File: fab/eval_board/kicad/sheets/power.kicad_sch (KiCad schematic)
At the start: 9 parts, among them J1 Barrel_Jack_12V, U10 ADP7118_0.9V, U11 TPS7A2018_1.8V_NCE, U12 TPS7A2010_1.0V, U13 TPS7A3301_3.3V, U14 TPS7A2018_1.8V_FPGA, U15 TPS54360

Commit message: fix: regenerate KiCad files in valid KiCad 8 format
- Rewrote all .kicad_sch files with proper lib_symbols sections,
  symbol instances, wires, hierarchical sheet references, and
  power port definitions (removed invalid ';;' comment syntax)
- Fixed .kicad_pcb: removed comment lines, added 922 missing net
  definitions, fixed gr_text justify format
- Regenerated Gerbers from fixed PCB using kicad-cli (30 files)
- All files validated with kicad-cli: schematic exports 5-page PDF,
  PCB exports SVG, DRC/ERC both run without parse errors
- Added regenerate_kicad.py generator script for reproducibility

Co-Authored-By: Bola Olatunji <bola.olatunji@ai.lightos.sh>
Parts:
- removed U11: TPS7A2018_1.8V_NCE, Package_TO_SOT_SMD:SOT-23-5, symbol Regulator_Linear:TPS7A20xx
- removed U12: TPS7A2010_1.0V, Package_TO_SOT_SMD:SOT-23-5, symbol Regulator_Linear:TPS7A20xx
- removed U14: TPS7A2018_1.8V_FPGA, Package_TO_SOT_SMD:SOT-23-5, symbol Regulator_Linear:TPS7A20xx
- added C1, C2, C3, C4, C5, C6: 100nF, Capacitor_SMD:C_0402_1005Metric, symbol Device:C
- added C20: 100uF, Capacitor_SMD:C_1206_3216Metric, symbol Device:C
- added D1: Green, LED_SMD:LED_0603_1608Metric, symbol Device:LED
- added R20: 1k, Resistor_SMD:R_0402_1005Metric, symbol Device:R
- added U11: TPS7A2018_3V3_1V8, Package_TO_SOT_SMD:SOT-23-5, symbol Regulator_Linear:TPS7A2018
- added U12: TPS7A2010_1V8_1V0, Package_TO_SOT_SMD:SOT-23-5, symbol Regulator_Linear:TPS7A2010
- added U14: TPS7A2018_3V3_1V8_FPGA, Package_TO_SOT_SMD:SOT-23-5, symbol Regulator_Linear:TPS7A2018
- L1: value 4.7uH -> 10uH; footprint Inductor_SMD:L_5x5mm -> Inductor_SMD:L_Wuerth_WE-LHMI_7050; MPN 744043004R7 -> 744373460100
- U10: value ADP7118_0.9V -> ADP7118_5V_0V9
- U13: value TPS7A3301_3.3V -> TPS7A3301_5V_3V3; footprint Package_TO_SOT_SMD:SOT-23-5 -> Package_TO_SOT_SMD:SOT-223-5; MPN TPS7A3301DBVR -> TPS7A3301DCQR
- U15: value TPS54360 -> TPS54360_12V_5V; MPN TPS54360DDAR -> TPS54360BDDAR
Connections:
- new net: F1.1, J1.1
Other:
- note removed: "POWER SEQUENCING: 12V → 5V (U15 buck, <1ms) 5V → 3.3V (U13 LDO, <0.5ms) 3.3V → 1.8V (U11/U14, <0.5ms) 1.8V → 1.0V (U12, <0.5ms) 5V → 0.9V (U10, <0.5ms) EN pins: tied to upstream rail for natural sequencing"
- note removed: "See BOM for complete capacitor placement. Decoupling: 100nF + 10uF per rail. Placement: Within 3mm of regulator output pin."
- title: Power Supply — LightRail Eval Board -> Power Supply - LightRail Eval Board

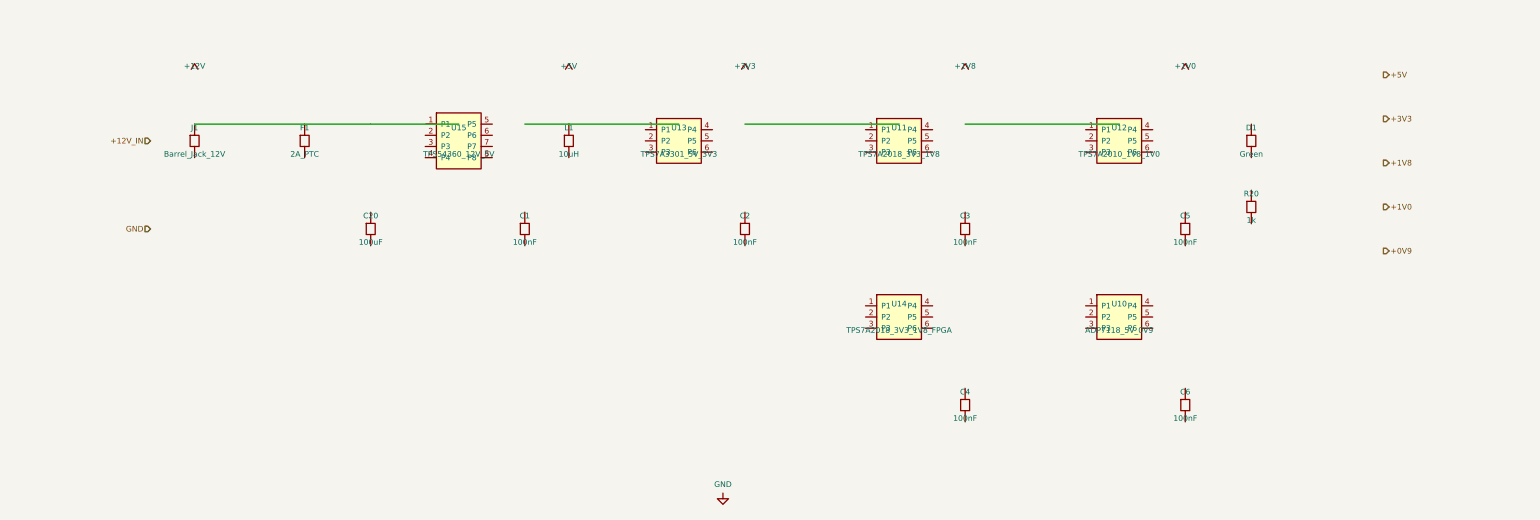
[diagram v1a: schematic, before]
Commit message: refactor: improve ERC quality via grid snapping and power flags
Co-Authored-By: Bola Olatunji <bola.olatunji@ai.lightos.sh>
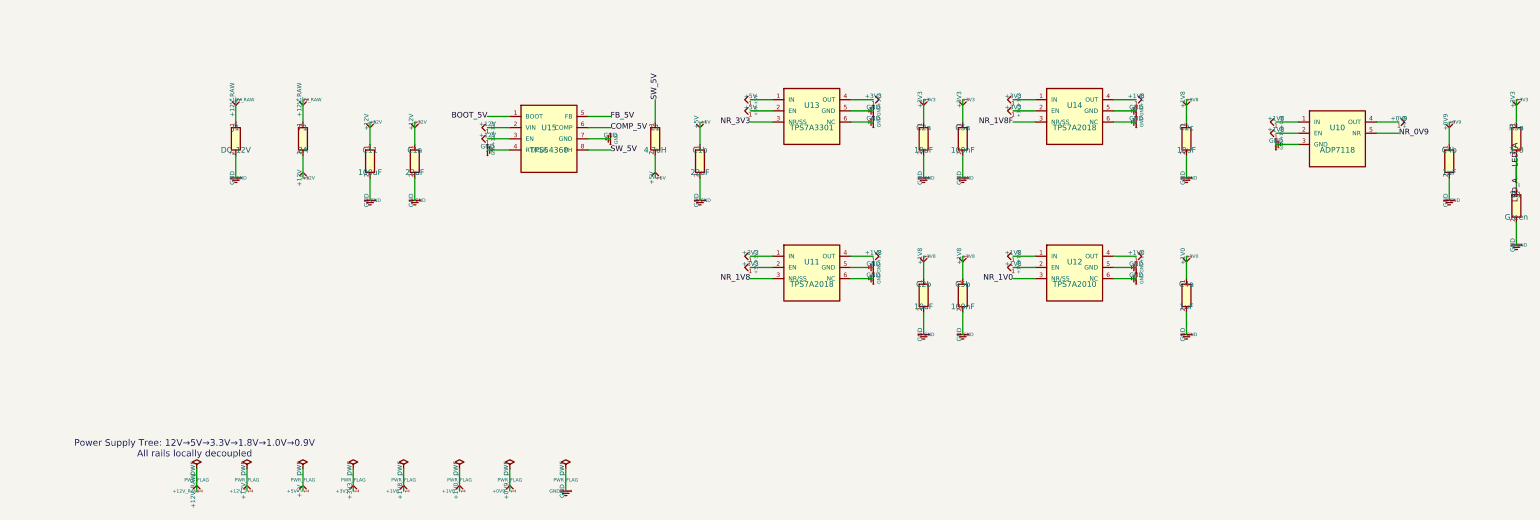
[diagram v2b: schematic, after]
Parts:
- removed C1, C2, C3, C4, C5, C6: 100nF, Capacitor_SMD:C_0402_1005Metric, symbol Device:C
- removed C20: 100uF, Capacitor_SMD:C_1206_3216Metric, symbol Device:C
- removed R20: 1k, Resistor_SMD:R_0402_1005Metric, symbol Device:R
- added C11: 100uF, Capacitor_SMD:C_7343, symbol Device:C
- added C1a, C1b: 22uF, Capacitor_SMD:C_0805, symbol Device:C
- added C2a, C2b, C2c: 10uF, Capacitor_SMD:C_0603, symbol Device:C
- added C4a, C4b: 1uF, Capacitor_SMD:C_0402, symbol Device:C
- added C5a, C5b: 100nF, Capacitor_SMD:C_0402, symbol Device:C
- added R5a: 330, Resistor_SMD:R_0402, symbol Device:R
- D1: footprint LED_SMD:LED_0603_1608Metric -> LED_SMD:LED_0603; MPN (none) -> 150060GS75000
- F1: value 2A_PTC -> 2A; footprint Fuse:Fuse_0805_2012Metric -> Fuse:Fuse_0805
- J1: value Barrel_Jack_12V -> DC_12V
- L1: value 10uH -> 4.7uH; footprint Inductor_SMD:L_Wuerth_WE-LHMI_7050 -> Inductor_SMD:L_5x5mm; MPN 744373460100 -> 744043004R7
- U10: value ADP7118_5V_0V9 -> ADP7118
- U11: value TPS7A2018_3V3_1V8 -> TPS7A2018
- U12: value TPS7A2010_1V8_1V0 -> TPS7A2010
- U13: value TPS7A3301_5V_3V3 -> TPS7A3301; footprint Package_TO_SOT_SMD:SOT-223-5 -> Package_TO_SOT_SMD:SOT-23-5; MPN TPS7A3301DCQR -> TPS7A3301DBVR
- U14: value TPS7A2018_3V3_1V8_FPGA -> TPS7A2018
- U15: value TPS54360_12V_5V -> TPS54360; footprint Package_SO:HSOP-8-1EP_3.9x4.9mm_P1.27mm_EP2.41x3.1mm -> Package_SO:HSOP-8; MPN TPS54360BDDAR -> TPS54360DDAR
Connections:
- net +0V9: now also U10.4 (OUT), C4b.1
- net +12V: now also F1.2, U15.2 (VIN), U15.3 (EN), C11.1, C1a.1
- net +1V0: now also U12.4 (OUT), C4a.1
- net +1V8: now also U10.1 (IN), U10.2 (EN), U11.4 (OUT), U12.1 (IN), U12.2 (EN), U14.4 (OUT), C2b.1, C2c.1, C5b.1
- net +3V3: now also U11.1 (IN), U11.2 (EN), U13.4 (OUT), U14.1 (IN), U14.2 (EN), C2a.1, C5a.1, R5a.1
- net +5V: now also L1.2, U13.1 (IN), U13.2 (EN), C1b.1
- net GND: now also D1.2, J1.2, U10.3 (GND), U11.5 (GND), U11.6 (NC), U12.5 (GND), U12.6 (NC), U13.5 (GND), U13.6 (NC), U14.5 (GND), U14.6 (NC), U15.4 (RT/CLK), U15.7 (GND), C11.2, C1a.2, C1b.2, C2a.2, C2b.2, C2c.2, C4a.2, C4b.2, C5a.2, C5b.2
- net +12V_RAW: now reaches F1.1, J1.1
- net NR_1V8F: now reaches U14.3 (NR/SS)
- net BOOT_5V: now reaches U15.1 (BOOT)
- net FB_5V: now reaches U15.5 (FB)
- net COMP_5V: now reaches U15.6 (COMP)
- net SW_5V: now reaches U15.8 (PH)
- net SW_5V: now also L1.1
- net NR_0V9: now reaches U10.5 (NR)
- net NR_1V0: now reaches U12.3 (NR/SS)
- net LED_A: now reaches D1.1
- net LED_A: now also R5a.2
- net NR_3V3: now reaches U13.3 (NR/SS)
- net NR_1V8: now reaches U11.3 (NR/SS)
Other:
- note added: "Power Supply Tree: 12V→5V→3.3V→1.8V→1.0V→0.9V All rails locally decoupled"
